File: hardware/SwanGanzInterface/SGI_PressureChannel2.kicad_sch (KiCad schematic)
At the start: 17 parts, among them U10 OPA2350, U6 INA122D

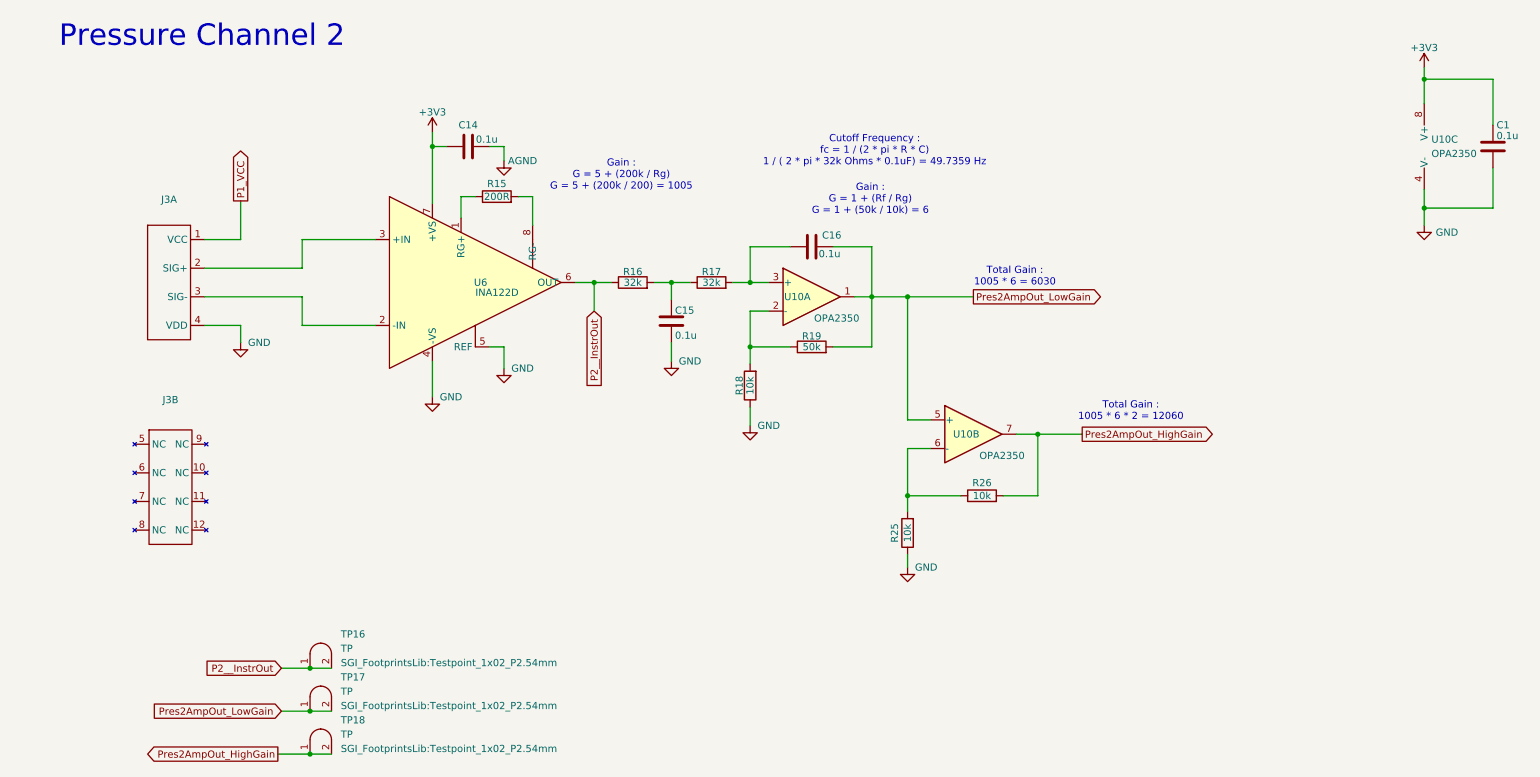
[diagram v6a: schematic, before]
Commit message: Routed Microcontroller Schematic Pins
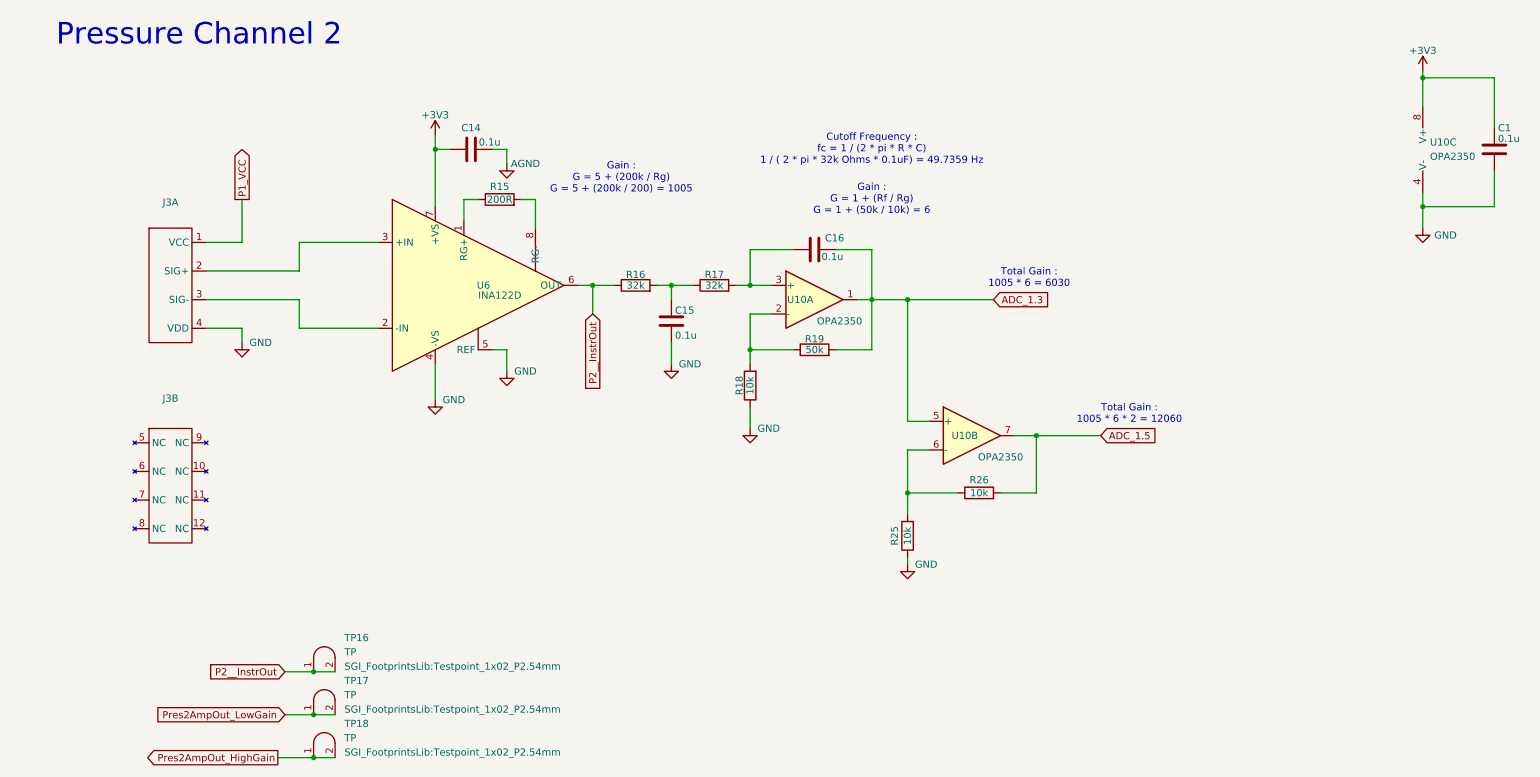
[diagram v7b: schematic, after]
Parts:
- C15, C16: footprint (none) -> Capacitor_SMD:C_1206_3216Metric
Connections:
- net Pres2AmpOut_HighGain: no longer R26.2, U10.7
- net Pres2AmpOut_LowGain: no longer C16.2, R19.2, U10.1, U10.5 (+)
- new net ADC_1.3: C16.2, R19.2, U10.1, U10.5 (+)
- new net ADC_1.5: R26.2, U10.7
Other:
- moved on the sheet: C1, C14, C16, J3A, R15, R16, R17, R19, R25, R26, TP16, TP17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

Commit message: Added Test Points to the Outputs of Analog Circuits
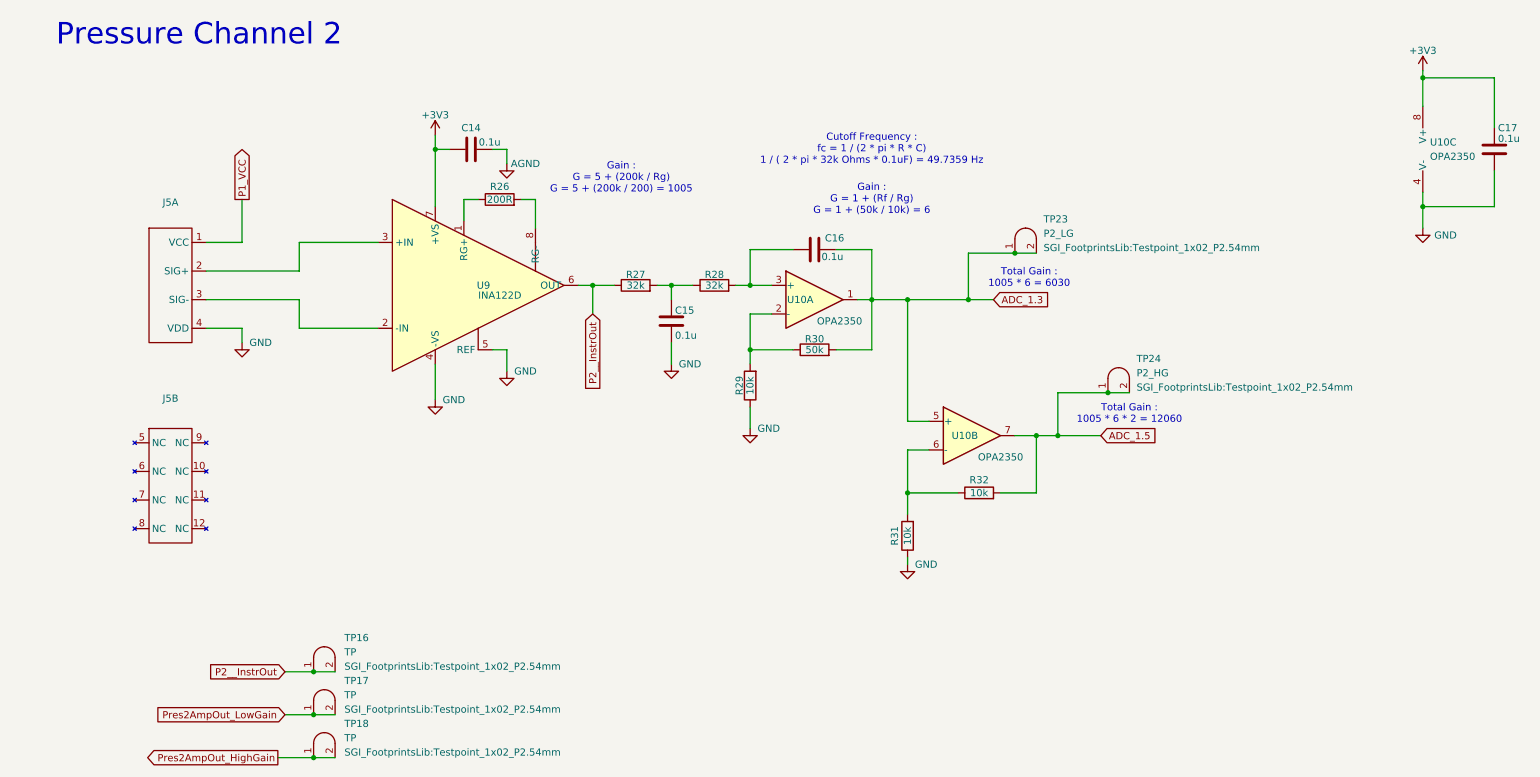
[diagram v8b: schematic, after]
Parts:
- added TP23: P2_LG, SGI_FootprintsLib:Testpoint_1x02_P2.54mm, symbol SGI_SymbolLib:Testpoint
- added TP24: P2_HG, SGI_FootprintsLib:Testpoint_1x02_P2.54mm, symbol SGI_SymbolLib:Testpoint
- C17: renamed from C1; footprint (none) -> Capacitor_SMD:C_0603_1608Metric
- renumbered J3 to J5, R15 to R26, R16 to R27, R17 to R28, R18 to R29, R19 to R30, R25 to R31, R26 to R32, U6 to U9
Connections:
- net ADC_1.3: now also TP23.1 (A), TP23.2 (B)
- net ADC_1.5: now also TP24.1 (A), TP24.2 (B)
